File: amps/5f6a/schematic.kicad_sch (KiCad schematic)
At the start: 64 parts, among them T3 2R sec

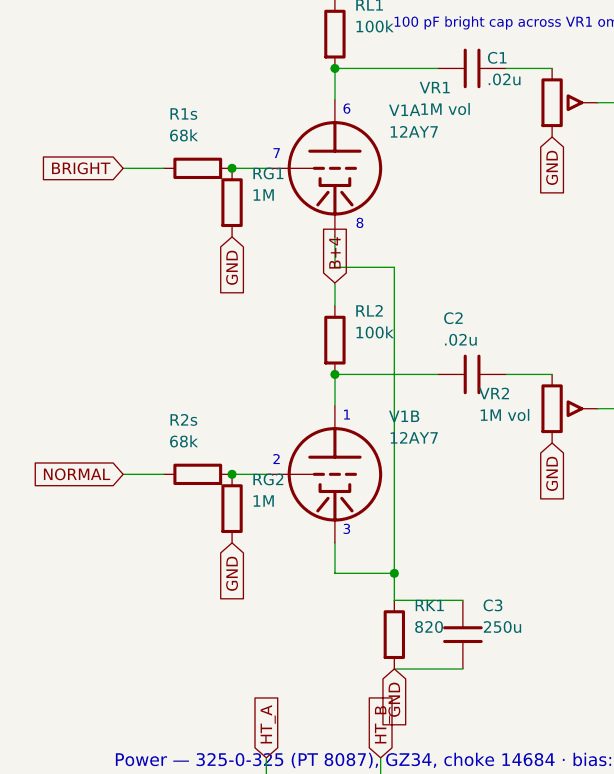
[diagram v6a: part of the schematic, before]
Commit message: Fix: draw the 5F6-A's 68k input stoppers on the board, and hang its 1M grid leaks at the jacks on the sheet
The 5F6-A layout (I-EG, 6600x5100) mounts the input stoppers at the board's right end, crop (4950,1350)-(6000,2900). Each 68K stands from a top eyelet that takes a jack lead down to the eyelet whose lead goes to the grid. The board omitted them: JB and JN ran straight to V1's grids, and the caption called the stoppers "drawn schematically or omitted". R1s and R2s now stand at cols 43 and 45, jack lead to the top eyelet and grid lead from the bottom one. The board grows 43 -> 46 cols. The output transformer's five leads move out to cols 45.6-46.2 so they clear the new column. series_bridge declares both stoppers to verify_layout_nets, as the AA764 and 5E4-A do.

The factory draws four 68Ks, one from each of the four input jacks. This board, like the schematic and bom.yaml ("the schematic draws one jack per channel (the chassis has four)"), carries one jack per channel. So it draws the stopper on that jack: jack 1, the one with the 1M across it. The caption now says so.

Placing the stoppers exposed a sheet error. The sheet hung RG1/RG2 on the grid side of the stoppers. Both factory pages put the 1M across jack 1, ahead of the 68Ks: on the schematic page at the jack-1 symbol, and on the layout page inside the jack-1 circle. The board already wired RG1/RG2 to the jacks. draw_5f6a.py now hangs them at the jack. The netlist is unchanged: the stoppers carry no DC, so RG1/RG2 stay on GAY1/GAY2. 5F6-A sheet-board: sheet_only_undeclared [R1s, R2s] -> [], no new findings, PASS. verify_schematic_nets PASS (claimed). Both board drawings, the sheet, site copies and og card are regenerated. FW-19 P10c.

Co-Authored-By: Claude Opus 5.5 <noreply@anthropic.com>
Claude-Session: https://claude.ai/code/session_01KBMfdh37HmCL2iWcBiL5J1
Signed-off-by: AnalogMaker <theanalogmaker@gmail.com>
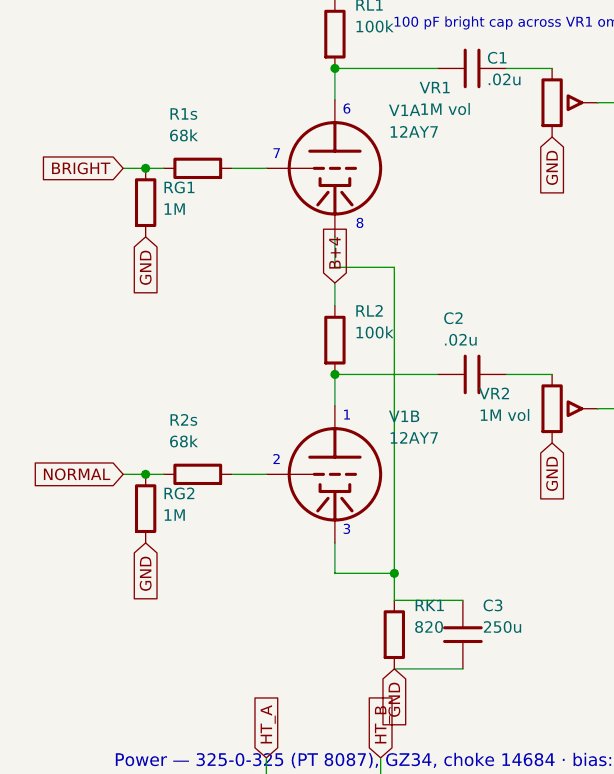
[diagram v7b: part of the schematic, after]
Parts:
- removed C12, C13: 20u, symbol cx:C
- removed C15b: 8u, symbol cx:C
- removed C2: .02u, symbol cx:C
- removed R2s: 68k, symbol cx:R
- removed RSL: 56k, symbol cx:R
- removed V3A: 12AX7, symbol cx:TRIODE
- added RB1: 15k, symbol cx:R
- added RD1: 4.7k, symbol cx:R
- added RD2: 10k, symbol cx:R
- added RLA: 82k 5%, symbol cx:R
- added V1B: 12AY7, symbol cx:TRIODE
- added VR2: 1M vol, symbol cx:POT
- added VR3: 250k treb, symbol cx:POT
- C12: renamed from RD1; value 4.7k -> 20u; symbol cx:R -> cx:C
- C13: renamed from RD2; value 10k -> 20u; symbol cx:R -> cx:C
- C15b: renamed from RB1; value 15k -> 8u; symbol cx:R -> cx:C
- C2: renamed from VR2; value 1M vol -> .02u; symbol cx:POT -> cx:C
- C4: renamed from VR3; value 250k treb -> 250p; symbol cx:POT -> cx:C
- R2s: renamed from V1B; value 12AY7 -> 68k; symbol cx:TRIODE -> cx:R
- RSL: renamed from C4; value 250p -> 56k; symbol cx:C -> cx:R
- V3A: renamed from V3B; Basing_unit 1 -> 2
- V3B: renamed from RLA; value 82k 5% -> 12AX7; symbol cx:R -> cx:TRIODE; Basing_unit (none) -> 1
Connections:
- net -48V: now also RB1.2; no longer C15b.2
- net B+2: now also RD1.1
- net B+3: now also RD1.2, RD2.1, RLA.1; no longer C12.2, V3B.1
- net B+4: now also RD2.2; no longer C13.2
- net BRIGHT: now also RG1.1
- net GND: now also C12.2, C13.2, C15b.2, VR2.3; no longer C2.3
- net NORMAL: now also R2s.1, RG2.1
- net at RL2.2: now also C2.1, V1B.1 (P); no longer R2s.1 (P)
- net at R1s.2, V1A.2 (G): no longer RG1.1
- net at C3.1, RK1.1, V1A.3 (K): now also V1B.3 (K); no longer R2s.3 (K)
- net at C5.1, C5b.1: now also RSL.2
- net at C5.2, VR4.1, VR4.2 (W): now also VR3.3; no longer C4.3
- net at RKCF.1, RSL.1, V2B.3 (K): now also C4.1
- net at C15b.1, D1.1 (A): now also RB1.1
- net at C9.1, RLB.2: now also V3B.1 (P); no longer V3A.1 (P)
- net at C6.2, RGA.1: now also V3A.2 (G)
- net at C8.1: now also V3A.1 (P), RLA.2; no longer V3B.2
- net at C7.1, RGB.2: now also V3B.2 (G); no longer V3A.2 (G)
- net at R2s.2: now also V1B.2 (G); no longer RG2.1
- net at C2.2: now also VR2.1; no longer RM2.1
- net at RTAIL.1, V3A.3 (K): now also V3B.3 (K)
- net at C6.1: now also VR3.2 (W); no longer C4.2 (W)
- new net: C4.2, VR3.1
- new net: RM2.1, VR2.2 (W)
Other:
- moved on the sheet: V3A
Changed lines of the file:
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@@
   (global_label "BRIGHT" (shape input) (at 19.6088 38.278 180)
     (effects (font (size 1.27 1.27)) (justify right)))
-  (wire (pts (xy 19.6088 38.278) (xy 24.0888 38.278))
+  (wire (pts (xy 19.6088 38.278) (xy 22.1088 38.278))
+    (stroke (width 0) (type default)))
+  (wire (pts (xy 22.1088 38.278) (xy 24.0888 38.278))
     (stroke (width 0) (type default)))
   (symbol (lib_id "cx:R") (at 27.8988 38.278 90) (unit 1)
@@
   (wire (pts (xy 31.7088 38.278) (xy 35.5188 38.278))
     (stroke (width 0) (type default)))
-  (junction (at 31.7088 38.278) (diameter 1.001) (color 0 0 0 0))
-  (symbol (lib_id "cx:R") (at 31.7088 42.088 0) (unit 1)
+  (junction (at 22.1088 38.278) (diameter 1.001) (color 0 0 0 0))
+  (symbol (lib_id "cx:R") (at 22.1088 42.088 0) (unit 1)
     (in_bom yes) (on_board yes)
-    (property "Reference" "RG1" (at 33.9088 38.888 0) (effects (font (size 1.27 1.27)) (justify left)))
-    (property "Value" "1M" (at 33.9088 41.288 0) (effects (font (size 1.27 1.27)) (justify left))))
-  (global_label "GND" (shape input) (at 31.7088 45.898 270)
+    (property "Reference" "RG1" (at 24.0248 40.448 0) (effects (font (size 1.27 1.27)) (justify left)))
+    (property "Value" "1M" (at 24.0248 42.848 0) (effects (font (size 1.27 1.27)) (justify left))))
+  (global_label "GND" (shape input) (at 22.1088 45.898 270)
     (effects (font (size 1.27 1.27)) (justify right)))
   (wire (pts (xy 43.1388 30.658) (xy 43.1388 27.178))
@@
   (global_label "NORMAL" (shape input) (at 19.6088 72.278 180)
     (effects (font (size 1.27 1.27)) (justify right)))
-  (wire (pts (xy 19.6088 72.278) (xy 24.0888 72.278))
+  (wire (pts (xy 19.6088 72.278) (xy 22.1088 72.278))
+    (stroke (width 0) (type default)))
+  (wire (pts (xy 22.1088 72.278) (xy 24.0888 72.278))
     (stroke (width 0) (type default)))
   (symbol (lib_id "cx:R") (at 27.8988 72.278 90) (unit 1)
@@
   (wire (pts (xy 31.7088 72.278) (xy 35.5188 72.278))
     (stroke (width 0) (type default)))
-  (junction (at 31.7088 72.278) (diameter 1.001) (color 0 0 0 0))
-  (symbol (lib_id "cx:R") (at 31.7088 76.088 0) (unit 1)
+  (junction (at 22.1088 72.278) (diameter 1.001) (color 0 0 0 0))
+  (symbol (lib_id "cx:R") (at 22.1088 76.088 0) (unit 1)
     (in_bom yes) (on_board yes)
-    (property "Reference" "RG2" (at 33.9088 72.888 0) (effects (font (size 1.27 1.27)) (justify left)))
-    (property "Value" "1M" (at 33.9088 75.288 0) (effects (font (size 1.27 1.27)) (justify left))))
-  (global_label "GND" (shape input) (at 31.7088 79.898 270)
+    (property "Reference" "RG2" (at 24.0248 74.448 0) (effects (font (size 1.27 1.27)) (justify left)))
+    (property "Value" "1M" (at 24.0248 76.848 0) (effects (font (size 1.27 1.27)) (justify left))))
+  (global_label "GND" (shape input) (at 22.1088 79.898 270)
     (effects (font (size 1.27 1.27)) (justify right)))
   (wire (pts (xy 43.1388 64.658) (xy 43.1388 61.178))

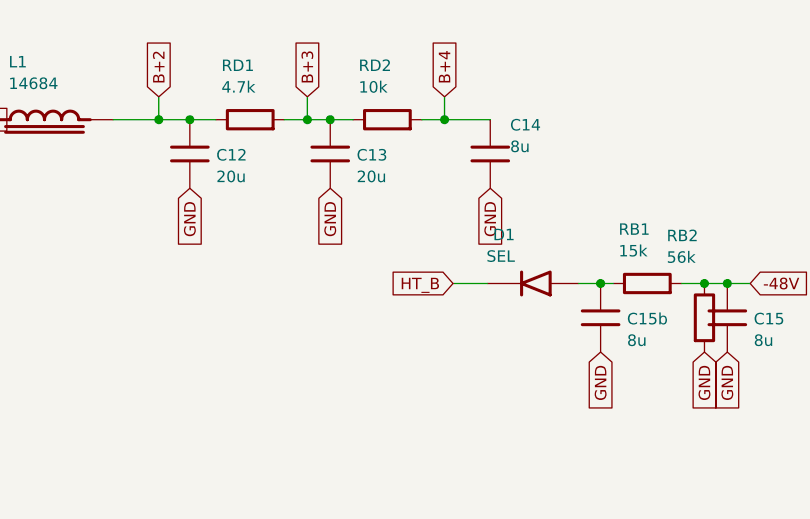
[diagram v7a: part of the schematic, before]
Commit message: Fix: the 5F6, 5F8-A and 5F6-A sheets fed the selenium bias rectifier from an HT end; it takes its own tap
All three factory schematics bring the bias feed down to its OWN winding terminal, between the upper HT end and the centre tap. It is not the HT end. At 3x zoom the vertical feed line crosses the upper "325 V AC" (5F8-A: "300 V AC") lead with no junction dot and ends on the next terminal down:
- 5F6 (F-EG) schematic page, crop (3560,3580)-(3900,3880), in the context of (3550,2850)-(4650,4100);
- 5F8-A (I-EG), native 6310x3506, crop (3250,2800)-(3800,3350);
- 5F6-A (I-EG), crop (3550,3500)-(4000,3950).
The layout pages agree. 5F6 crop (900,2200)-(2900,3800) and 5F8-A crop (600,1300)-(2400,2000) each draw a dedicated RED-BLUE transformer lead to SEL. RECT. "+", separate from the two RED HT leads that go to the rectifier plates.

So red-blue is a separate tap, as on the 6G6-B, and the sheets were the surface in error: each lettered D1's anode HT_B, putting the bias rectifier on the rectifier plate node. Each sheet now letters it HT_TAP. sch_map.yaml winding_labels declares HT_TAP: tap, so the UNFED RECTIFIER walk still sees D1 fed, and HT_B's note drops "also feeds bias rectifier D1". The 5F6 and 5F8-A boards, which wire PT.red-blue to D1, declare net_map.leads "<HT_TAP>": PT.red-blue. The 5F6-A board does not place D1 (a declared not_on_board), so it needs no lead.

Sheet-board: 5F6 misplaced [D1] -> [] (both drawings claim verified; it now PASSes), 5F8-A misplaced [D1] -> []. verify_schematic_nets PASS for all three, and 48/48 rectifiers fed. No netlist change: the bias supply is the ideal NBIAS source in every netlist. FW-19 P10c.

Co-Authored-By: Claude Opus 5.5 <noreply@anthropic.com>
Claude-Session: https://claude.ai/code/session_01KBMfdh37HmCL2iWcBiL5J1
Signed-off-by: AnalogMaker <theanalogmaker@gmail.com>
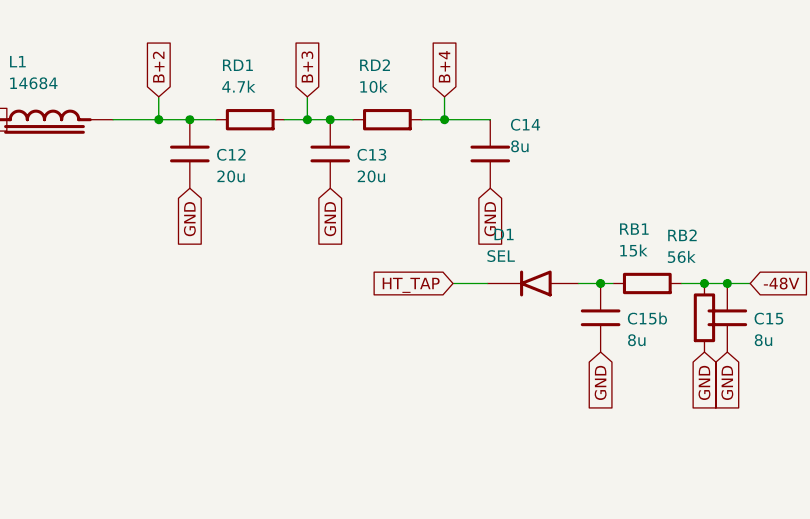
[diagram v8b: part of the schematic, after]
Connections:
- net HT_B: no longer D1.2 (K)
- new net HT_TAP: D1.2 (K)
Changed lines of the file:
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@@
   (global_label "GND" (shape input) (at 135.849 131.698 270)
     (effects (font (size 1.27 1.27)) (justify right)))
-  (global_label "HT_B" (shape input) (at 131.709 142.278 180)
+  (global_label "HT_TAP" (shape input) (at 131.709 142.278 180)
     (effects (font (size 1.27 1.27)) (justify right)))
   (wire (pts (xy 131.709 142.278) (xy 135.519 142.278))
